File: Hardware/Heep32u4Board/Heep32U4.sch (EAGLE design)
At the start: 8 parts, among them J2 AVR_SPI_PROG_3X2PTH, U1 ENC28J60-SO, Y1 16MHz

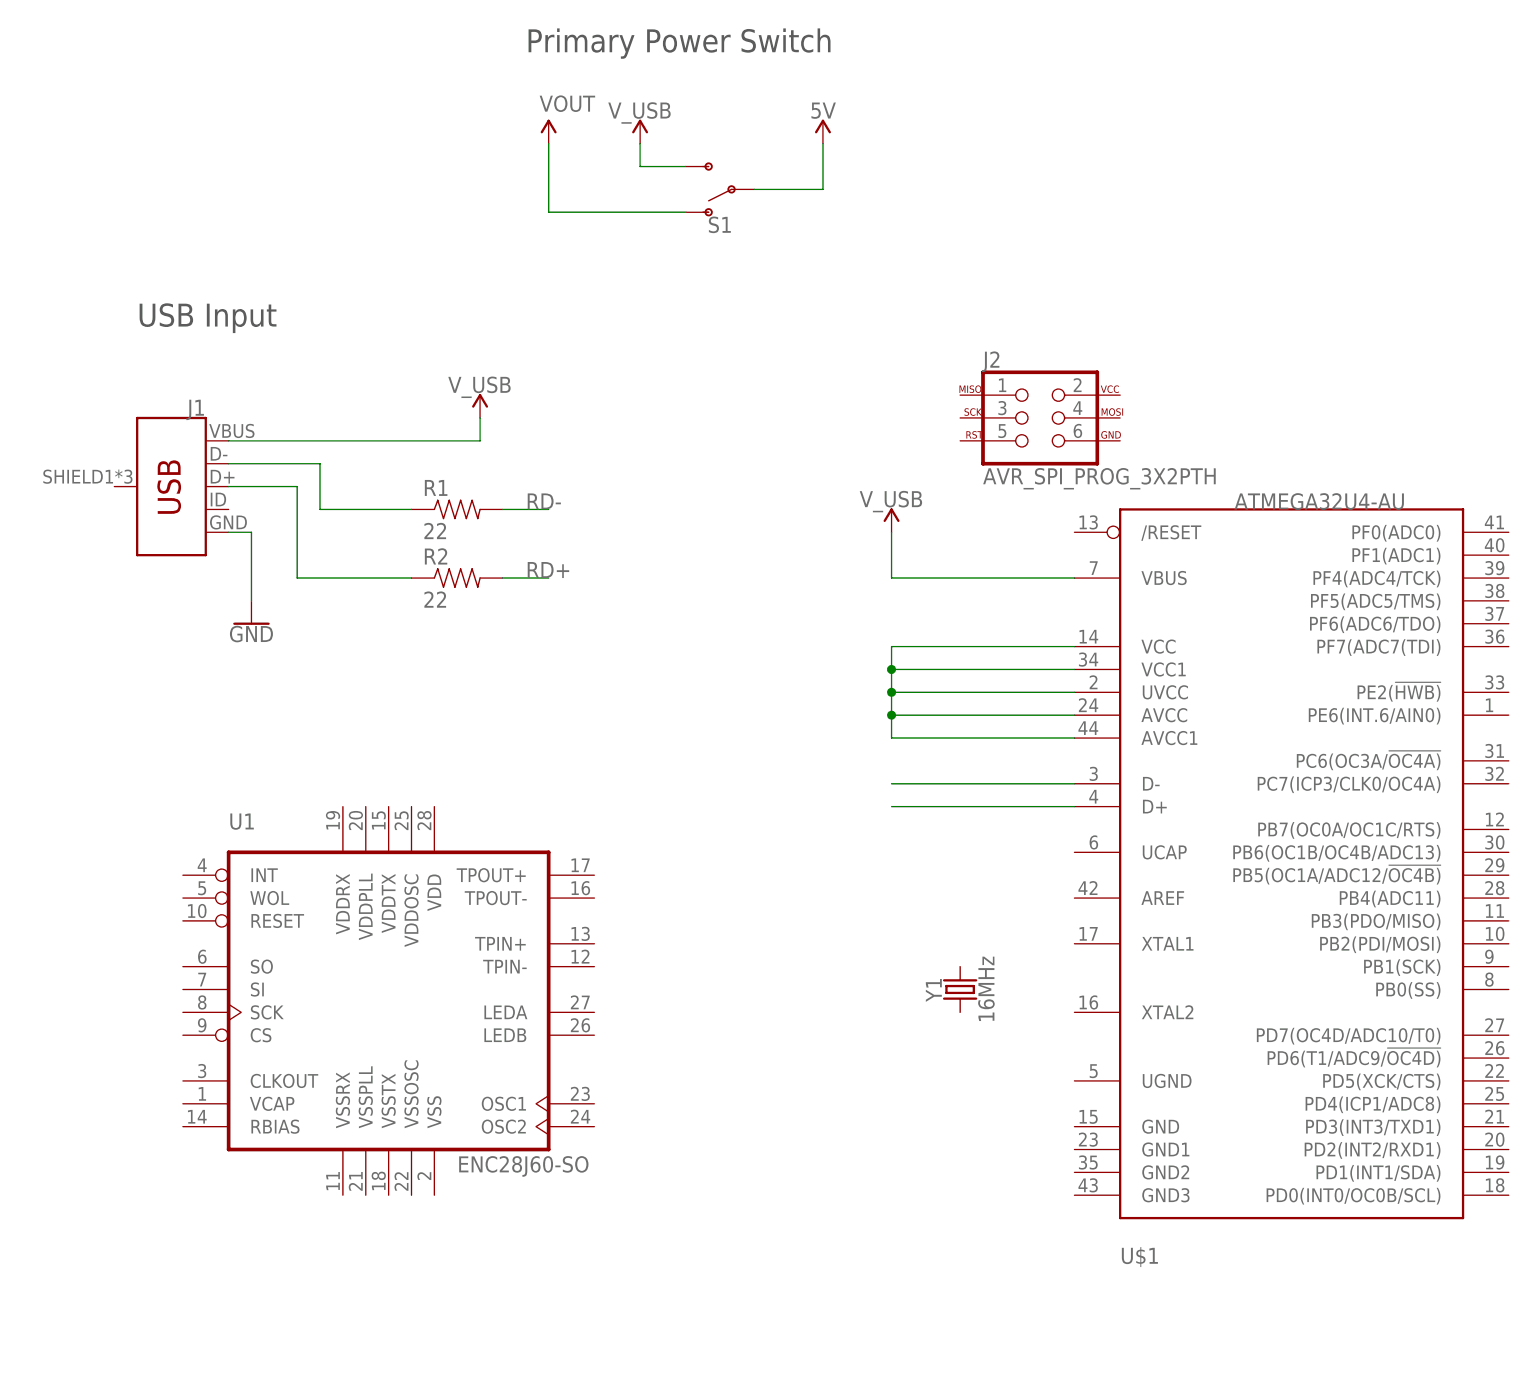
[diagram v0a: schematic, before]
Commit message: #20 Added USB inputs and crystal
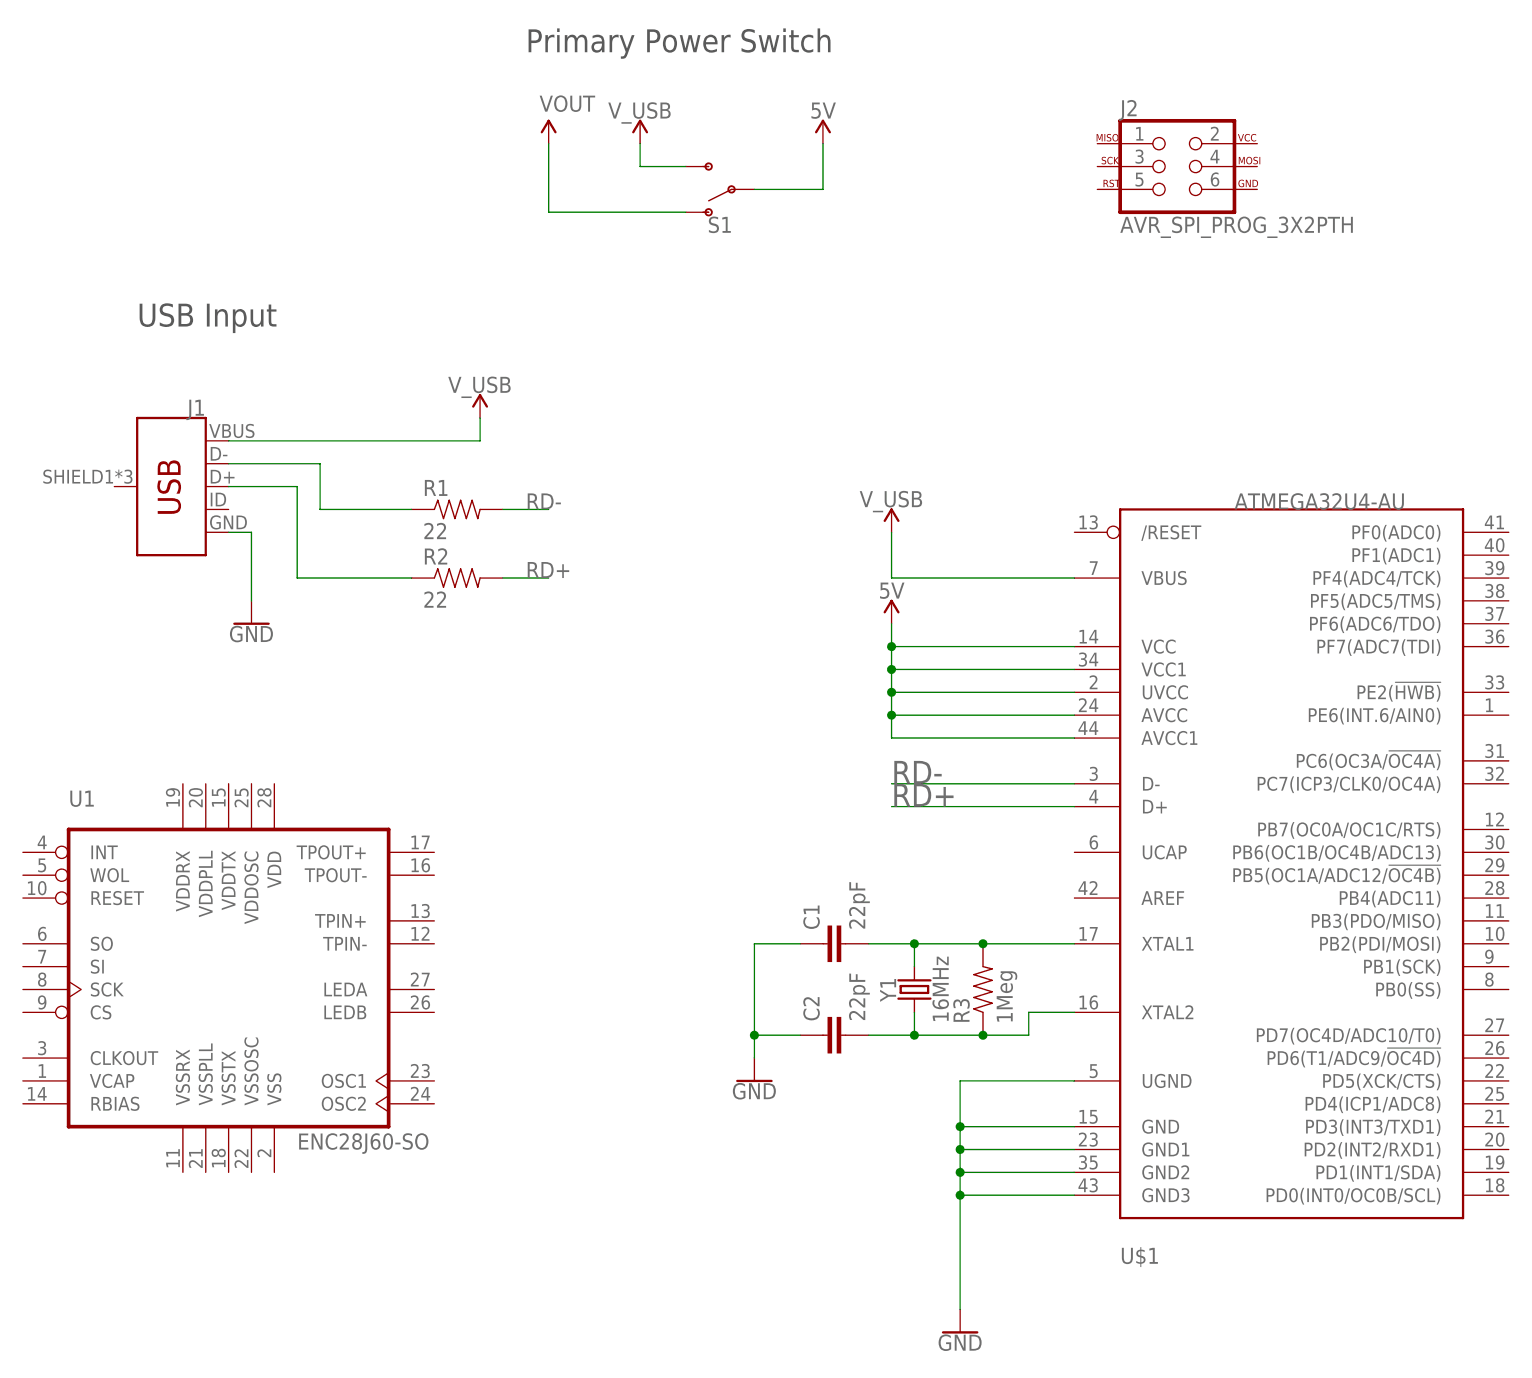
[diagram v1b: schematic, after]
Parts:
- added C1, C2: 22pF, SparkFun-Passives:CAP0603-CAP
- added R3: 1Meg, SparkFun-Passives:RESISTOR0603-RES
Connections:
- removed net N$1: U$1.AVCC, U$1.AVCC1, U$1.UVCC, U$1.VCC, U$1.VCC1
- removed net N$2: U$1.D-
- removed net N$5: U$1.D+
- new net N$10: C2.2, R3.1, U$1.XTAL2, Y1.1
- new net N$9: C1.2, R3.2, U$1.XTAL1, Y1.2
- net 5V: now also U$1.AVCC, U$1.AVCC1, U$1.UVCC, U$1.VCC, U$1.VCC1
- net GND: now also C1.1, C2.1, U$1.GND, U$1.GND1, U$1.GND2, U$1.GND3, U$1.UGND
- net RD+: now also U$1.D+
- net RD-: now also U$1.D-
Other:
- moved on the sheet: J2, U1, Y1
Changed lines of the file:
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@@
 <part name="SUPPLY4" library="SparkFun-PowerSymbols" deviceset="5V" device=""/>
 <part name="SUPPLY5" library="SparkFun-PowerSymbols" deviceset="VOUT" device=""/>
+<part name="SUPPLY6" library="SparkFun-PowerSymbols" deviceset="5V" device=""/>
+<part name="R3" library="SparkFun-Passives" deviceset="RESISTOR" device="0603-RES" value="1Meg"/>
+<part name="C1" library="SparkFun-Passives" deviceset="CAP" device="0603-CAP" value="22pF"/>
+<part name="C2" library="SparkFun-Passives" deviceset="CAP" device="0603-CAP" value="22pF"/>
+<part name="GND2" library="SparkFun-PowerSymbols" deviceset="GND" device=""/>
+<part name="GND3" library="SparkFun-PowerSymbols" deviceset="GND" device=""/>
 </parts>
 <sheets>
@@
 <instances>
 <instance part="U$1" gate="G$1" x="106.68" y="43.18"/>
-<instance part="U1" gate="G$1" x="10.16" y="30.48"/>
+<instance part="U1" gate="G$1" x="-7.62" y="33.02"/>
 <instance part="J1" gate="G$1" x="-15.24" y="91.44" rot="MR0"/>
-<instance part="Y1" gate="G$1" x="71.12" y="35.56" rot="R90"/>
-<instance part="J2" gate="G$1" x="78.74" y="99.06"/>
+<instance part="Y1" gate="G$1" x="66.04" y="35.56" rot="R90"/>
+<instance part="J2" gate="G$1" x="93.98" y="127"/>
 <instance part="R1" gate="G$1" x="15.24" y="88.9"/>
 <instance part="R2" gate="G$1" x="15.24" y="81.28"/>
@@
 <instance part="SUPPLY4" gate="G$1" x="55.88" y="129.54"/>
 <instance part="SUPPLY5" gate="G$1" x="25.4" y="129.54"/>
+<instance part="SUPPLY6" gate="G$1" x="63.5" y="76.2"/>
+<instance part="R3" gate="G$1" x="73.66" y="35.56" rot="R90"/>
+<instance part="C1" gate="G$1" x="58.42" y="40.64" rot="R90"/>
+<instance part="C2" gate="G$1" x="58.42" y="30.48" rot="R90"/>
+<instance part="GND2" gate="1" x="48.26" y="25.4"/>
+<instance part="GND3" gate="1" x="71.12" y="-2.54"/>
 </instances>
 <busses>
@@
 <label x="22.86" y="88.9" size="1.778" layer="95"/>
 </segment>
+<segment>
+<pinref part="U$1" gate="G$1" pin="D-"/>
+<wire x1="83.82" y1="58.42" x2="63.5" y2="58.42" width="0.1524" layer="91"/>
+<label x="63.5" y="58.42" size="2.54" layer="95"/>
+</segment>
 </net>
 <net name="RD+" class="0">
@@
 <wire x1="20.32" y1="81.28" x2="25.4" y2="81.28" width="0.1524" layer="91"/>
 <label x="22.86" y="81.28" size="1.778" layer="95"/>
+</segment>
+<segment>
+<pinref part="U$1" gate="G$1" pin="D+"/>
+<wire x1="83.82" y1="55.88" x2="63.5" y2="55.88" width="0.1524" layer="91"/>
+<label x="63.5" y="55.88" size="2.54" layer="95"/>
 </segment>
 </net>
@@
 <pinref part="GND1" gate="1" pin="GND"/>
 </segment>
-</net>
-<net name="N$1" class="0">
+<segment>
+<pinref part="C1" gate="G$1" pin="1"/>
+<wire x1="53.34" y1="40.64" x2="48.26" y2="40.64" width="0.1524" layer="91"/>
+<wire x1="48.26" y1="40.64" x2="48.26" y2="30.48" width="0.1524" layer="91"/>
+<pinref part="C2" gate="G$1" pin="1"/>
+<wire x1="48.26" y1="30.48" x2="53.34" y2="30.48" width="0.1524" layer="91"/>
+<wire x1="48.26" y1="30.48" x2="48.26" y2="27.94" width="0.1524" layer="91"/>
+<junction x="48.26" y="30.48"/>
+<pinref part="GND2" gate="1" pin="GND"/>
+</segment>
+<segment>
+<pinref part="U$1" gate="G$1" pin="GND"/>
+<wire x1="83.82" y1="20.32" x2="71.12" y2="20.32" width="0.1524" layer="91"/>
+<wire x1="71.12" y1="20.32" x2="71.12" y2="17.78" width="0.1524" layer="91"/>
+<pinref part="U$1" gate="G$1" pin="GND1"/>
+<wire x1="71.12" y1="17.78" x2="71.12" y2="15.24" width="0.1524" layer="91"/>
+<wire x1="71.12" y1="15.24" x2="71.12" y2="12.7" width="0.1524" layer="91"/>
+<wire x1="71.12" y1="12.7" x2="71.12" y2="0" width="0.1524" layer="91"/>
+<wire x1="83.82" y1="17.78" x2="71.12" y2="17.78" width="0.1524" layer="91"/>
+<junction x="71.12" y="17.78"/>
+<pinref part="U$1" gate="G$1" pin="GND2"/>
+<wire x1="83.82" y1="15.24" x2="71.12" y2="15.24" width="0.1524" layer="91"/>
+<junction x="71.12" y="15.24"/>
+<pinref part="U$1" gate="G$1" pin="GND3"/>
+<wire x1="83.82" y1="12.7" x2="71.12" y2="12.7" width="0.1524" layer="91"/>
+<junction x="71.12" y="12.7"/>
+<pinref part="U$1" gate="G$1" pin="UGND"/>
+<wire x1="83.82" y1="25.4" x2="71.12" y2="25.4" width="0.1524" layer="91"/>
+<wire x1="71.12" y1="25.4" x2="71.12" y2="20.32" width="0.1524" layer="91"/>
+<junction x="71.12" y="20.32"/>
+<pinref part="GND3" gate="1" pin="GND"/>
+</segment>
+</net>
+<net name="5V" class="0">
+<segment>
+<pinref part="S1" gate="1" pin="P"/>
+<wire x1="48.26" y1="124.46" x2="55.88" y2="124.46" width="0.1524" layer="91"/>
+<wire x1="55.88" y1="124.46" x2="55.88" y2="129.54" width="0.1524" layer="91"/>
+<pinref part="SUPPLY4" gate="G$1" pin="5V"/>
+</segment>
 <segment>
 <pinref part="U$1" gate="G$1" pin="VCC"/>
@@
 <wire x1="83.82" y1="68.58" x2="63.5" y2="68.58" width="0.1524" layer="91"/>
 <junction x="63.5" y="68.58"/>
-</segment>
-</net>
-<net name="N$2" class="0">
-<segment>
-<pinref part="U$1" gate="G$1" pin="D-"/>
-<wire x1="83.82" y1="58.42" x2="63.5" y2="58.42" width="0.1524" layer="91"/>
-</segment>
-</net>
-<net name="N$5" class="0">
-<segment>
-<pinref part="U$1" gate="G$1" pin="D+"/>
-<wire x1="83.82" y1="55.88" x2="63.5" y2="55.88" width="0.1524" layer="91"/>
-</segment>
-</net>
-<net name="5V" class="0">
-<segment>
-<pinref part="S1" gate="1" pin="P"/>
-<wire x1="48.26" y1="124.46" x2="55.88" y2="124.46" width="0.1524" layer="91"/>
-<wire x1="55.88" y1="124.46" x2="55.88" y2="129.54" width="0.1524" layer="91"/>
-<pinref part="SUPPLY4" gate="G$1" pin="5V"/>
+<wire x1="63.5" y1="73.66" x2="63.5" y2="76.2" width="0.1524" layer="91"/>
+<junction x="63.5" y="73.66"/>
+<pinref part="SUPPLY6" gate="G$1" pin="5V"/>
 </segment>
 </net>
@@
 </segment>
 </net>
+<net name="N$9" class="0">
+<segment>
+<pinref part="U$1" gate="G$1" pin="XTAL1"/>
+<pinref part="R3" gate="G$1" pin="2"/>
+<wire x1="83.82" y1="40.64" x2="73.66" y2="40.64" width="0.1524" layer="91"/>
+<pinref part="Y1" gate="G$1" pin="2"/>
+<wire x1="73.66" y1="40.64" x2="66.04" y2="40.64" width="0.1524" layer="91"/>
+<wire x1="66.04" y1="40.64" x2="66.04" y2="38.1" width="0.1524" layer="91"/>
+<junction x="73.66" y="40.64"/>
+<pinref part="C1" gate="G$1" pin="2"/>
+<wire x1="66.04" y1="40.64" x2="60.96" y2="40.64" width="0.1524" layer="91"/>
+<junction x="66.04" y="40.64"/>
+</segment>
+</net>
+<net name="N$10" class="0">
+<segment>
+<pinref part="R3" gate="G$1" pin="1"/>
+<pinref part="Y1" gate="G$1" pin="1"/>
+<wire x1="73.66" y1="30.48" x2="66.04" y2="30.48" width="0.1524" layer="91"/>
+<wire x1="66.04" y1="30.48" x2="66.04" y2="33.02" width="0.1524" layer="91"/>
+<pinref part="U$1" gate="G$1" pin="XTAL2"/>
+<wire x1="83.82" y1="33.02" x2="78.74" y2="33.02" width="0.1524" layer="91"/>
+<wire x1="78.74" y1="33.02" x2="78.74" y2="30.48" width="0.1524" layer="91"/>
+<wire x1="78.74" y1="30.48" x2="73.66" y2="30.48" width="0.1524" layer="91"/>
+<junction x="73.66" y="30.48"/>
+<pinref part="C2" gate="G$1" pin="2"/>
+<wire x1="66.04" y1="30.48" x2="60.96" y2="30.48" width="0.1524" layer="91"/>
+<junction x="66.04" y="30.48"/>
+</segment>
+</net>
